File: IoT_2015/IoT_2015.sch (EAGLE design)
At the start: 31 parts, among them Y1 ABLS-16.000MHZ-B4-T

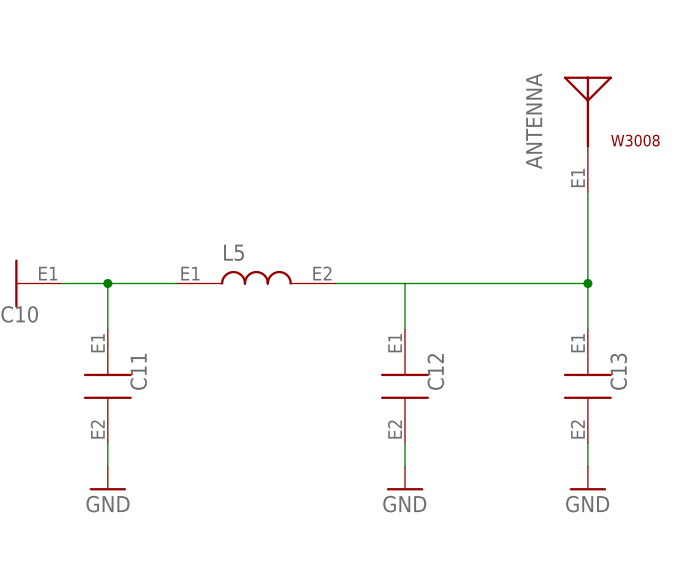
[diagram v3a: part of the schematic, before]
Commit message: Correction with ERC
Correction carried out with ERC
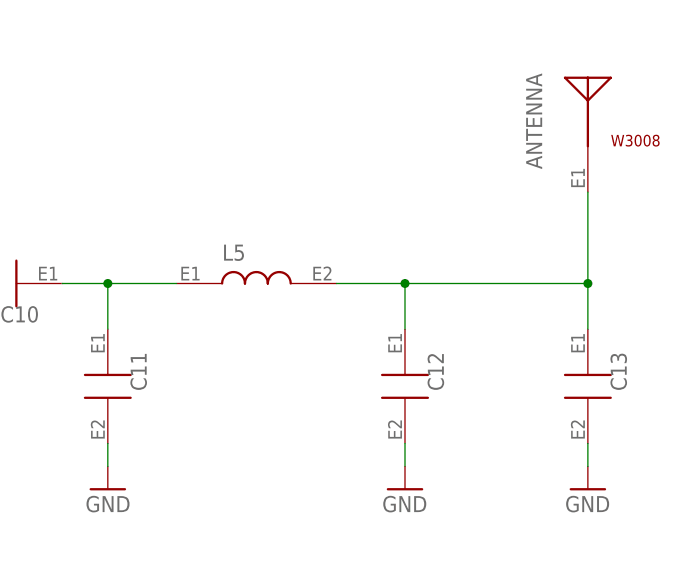
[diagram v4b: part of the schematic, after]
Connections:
- net GND: now also C13.E2
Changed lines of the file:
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@@
-</segment>
-<segment>
-<wire x1="307.34" y1="25.4" x2="307.34" y2="27.94" width="0.1524" layer="91"/>
 </segment>
 <segment>
@@
 <pinref part="R2" gate="G$1" pin="E1"/>
 <pinref part="GND13" gate="1" pin="GND"/>
+</segment>
+<segment>
+<pinref part="GND12" gate="1" pin="GND"/>
+<pinref part="C13" gate="G$1" pin="E2"/>
+<wire x1="307.34" y1="25.4" x2="307.34" y2="27.94" width="0.1524" layer="91"/>
 </segment>
 </net>
@@
 <wire x1="307.34" y1="45.72" x2="307.34" y2="55.88" width="0.1524" layer="91"/>
 <junction x="307.34" y="45.72"/>
+<junction x="287.02" y="45.72"/>
 </segment>
 </net>

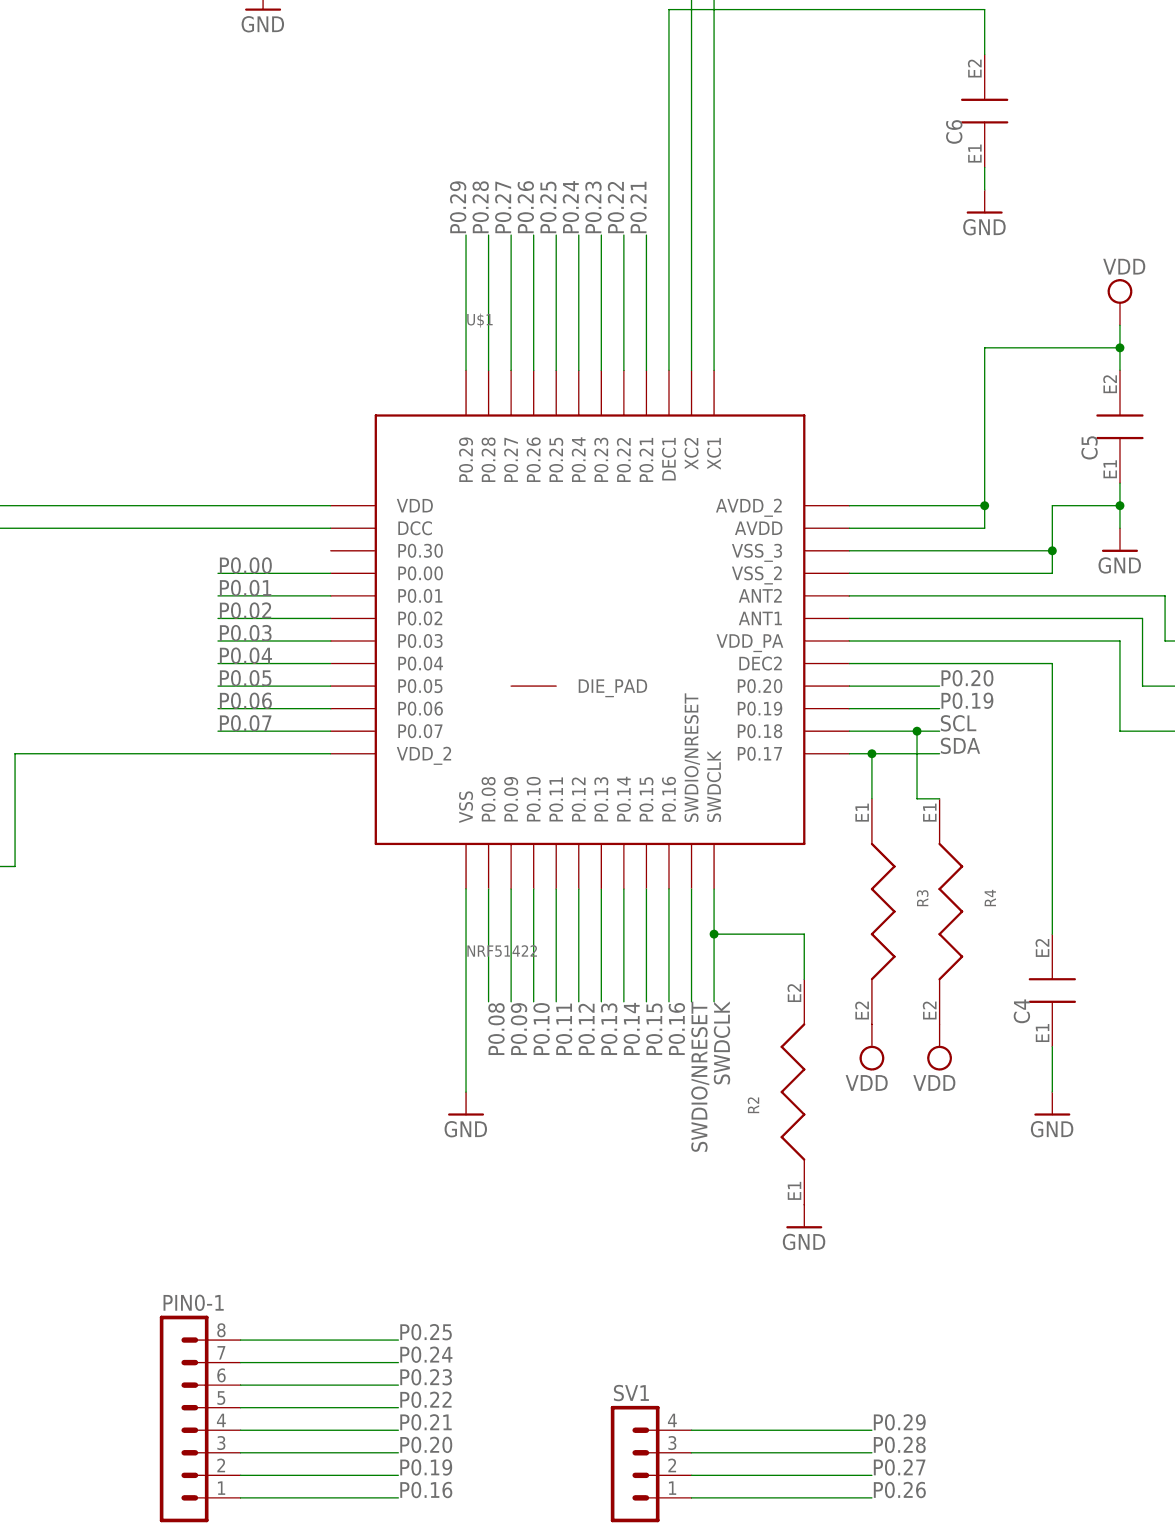
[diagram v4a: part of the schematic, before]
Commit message: BoardLayout
Fixed the layer-property of battery and started the board-layout.
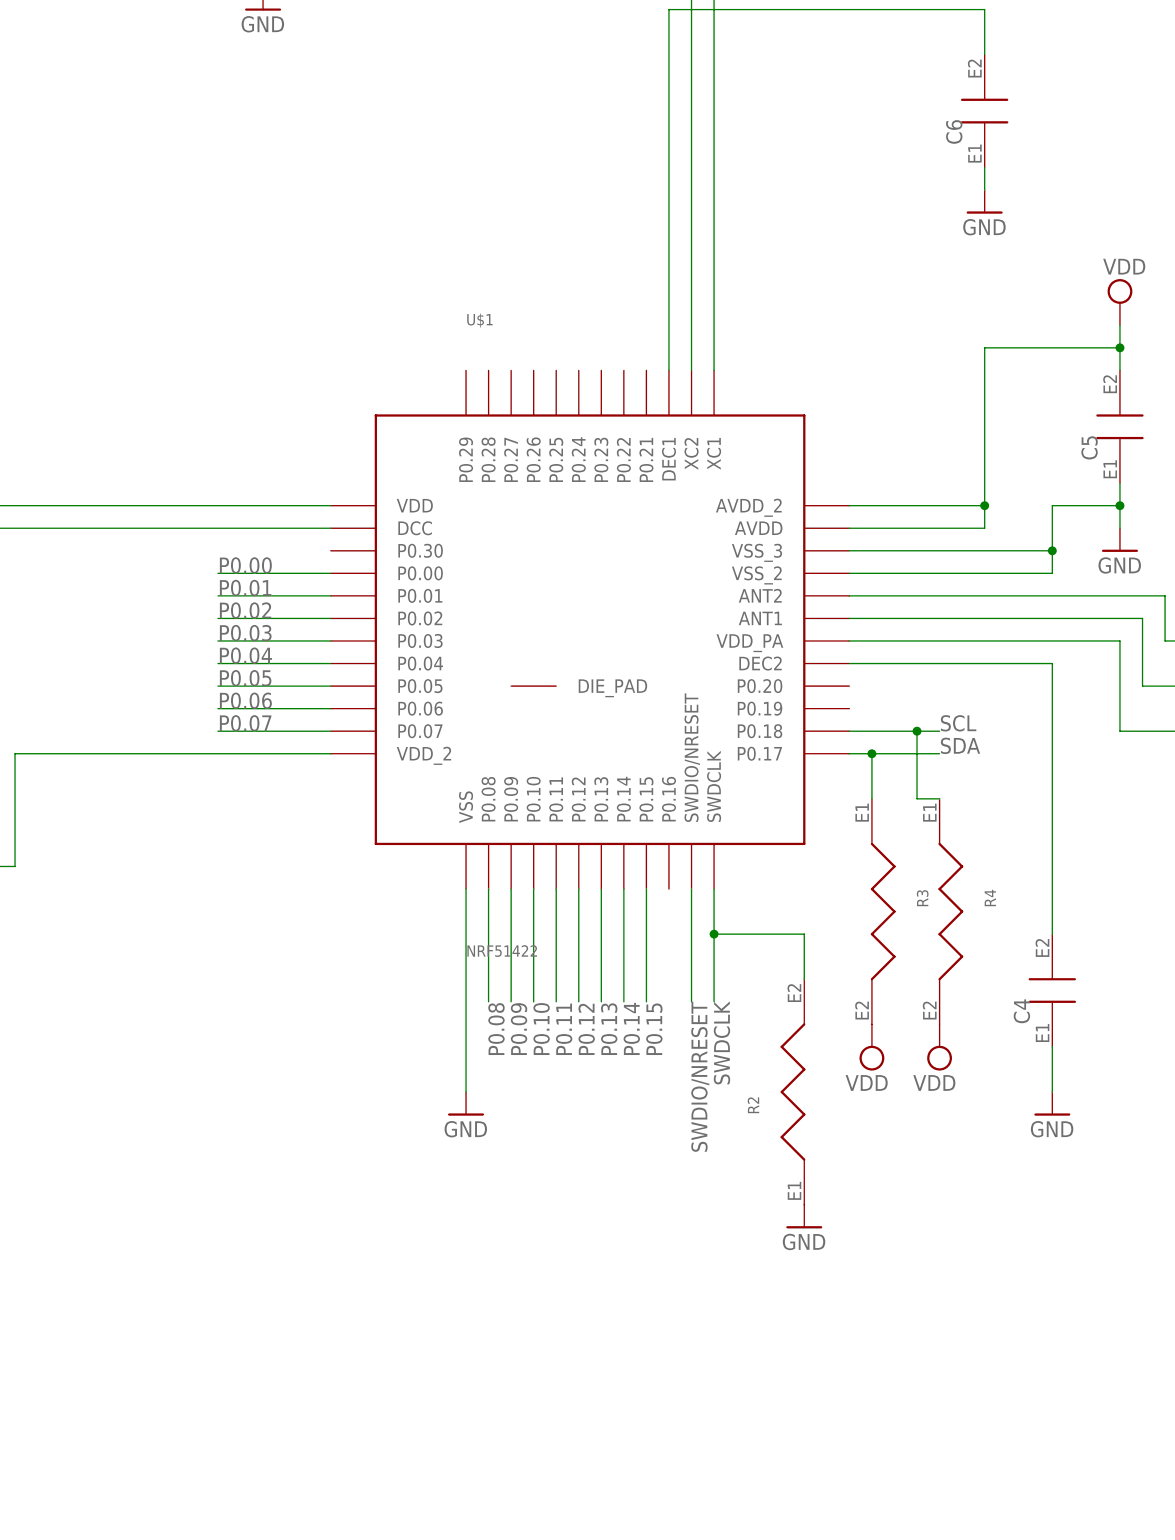
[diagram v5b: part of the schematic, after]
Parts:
- removed PIN0-1: (no value), con-lstb:MA08-1
- removed SV1: (no value), con-lstb:MA04-1
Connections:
- removed net P0.16: PIN0-1.1, U$1.P0.16
- removed net P0.19: PIN0-1.2, U$1.P0.19
- removed net P0.20: PIN0-1.3, U$1.P0.20
- removed net P0.21: PIN0-1.4, U$1.P0.21
- removed net P0.22: PIN0-1.5, U$1.P0.22
- removed net P0.23: PIN0-1.6, U$1.P0.23
- removed net P0.24: PIN0-1.7, U$1.P0.24
- removed net P0.25: PIN0-1.8, U$1.P0.25
- removed net P0.26: SV1.1, U$1.P0.26
- removed net P0.27: SV1.2, U$1.P0.27
- removed net P0.28: SV1.3, U$1.P0.28
- removed net P0.29: SV1.4, U$1.P0.29
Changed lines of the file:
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@@
 <part name="SUPPLY7" library="supply2" deviceset="VDD" device=""/>
 <part name="SUPPLY8" library="supply2" deviceset="VDD" device=""/>
-<part name="PIN0-1" library="con-lstb" deviceset="MA08-1" device=""/>
-<part name="SV1" library="con-lstb" deviceset="MA04-1" device=""/>
 </parts>
 <sheets>
@@
 <instance part="SUPPLY7" gate="G$1" x="129.54" y="0" rot="R180"/>
 <instance part="SUPPLY8" gate="G$1" x="137.16" y="0" rot="R180"/>
-<instance part="PIN0-1" gate="1" x="50.8" y="-43.18"/>
-<instance part="SV1" gate="1" x="101.6" y="-45.72"/>
 </instances>
 <busses>
@@
 </segment>
 </net>
-<net name="P0.16" class="0">
-<segment>
-<pinref part="U$1" gate="G$1" pin="P0.16"/>
-<wire x1="106.68" y1="17.78" x2="106.68" y2="5.08" width="0.1524" layer="91"/>
-<label x="106.68" y="5.08" size="1.778" layer="95" rot="R270"/>
-</segment>
-<segment>
-<pinref part="PIN0-1" gate="1" pin="1"/>
-<wire x1="58.42" y1="-50.8" x2="76.2" y2="-50.8" width="0.1524" layer="91"/>
-<label x="76.2" y="-50.8" size="1.778" layer="95"/>
-</segment>
-</net>
-<net name="P0.19" class="0">
-<segment>
-<pinref part="U$1" gate="G$1" pin="P0.19"/>
-<wire x1="127" y1="38.1" x2="137.16" y2="38.1" width="0.1524" layer="91"/>
-<label x="137.16" y="38.1" size="1.778" layer="95"/>
-</segment>
-<segment>
-<pinref part="PIN0-1" gate="1" pin="2"/>
-<wire x1="58.42" y1="-48.26" x2="76.2" y2="-48.26" width="0.1524" layer="91"/>
-<label x="76.2" y="-48.26" size="1.778" layer="95"/>
-</segment>
-</net>
-<net name="P0.20" class="0">
-<segment>
-<pinref part="U$1" gate="G$1" pin="P0.20"/>
-<wire x1="127" y1="40.64" x2="137.16" y2="40.64" width="0.1524" layer="91"/>
-<label x="137.16" y="40.64" size="1.778" layer="95"/>
-</segment>
-<segment>
-<pinref part="PIN0-1" gate="1" pin="3"/>
-<wire x1="58.42" y1="-45.72" x2="76.2" y2="-45.72" width="0.1524" layer="91"/>
-<label x="76.2" y="-45.72" size="1.778" layer="95"/>
-</segment>
-</net>
-<net name="P0.21" class="0">
-<segment>
-<pinref part="U$1" gate="G$1" pin="P0.21"/>
-<wire x1="104.14" y1="76.2" x2="104.14" y2="91.44" width="0.1524" layer="91"/>
-<label x="104.14" y="91.44" size="1.778" layer="95" rot="R90"/>
-</segment>
-<segment>
-<pinref part="PIN0-1" gate="1" pin="4"/>
-<wire x1="58.42" y1="-43.18" x2="76.2" y2="-43.18" width="0.1524" layer="91"/>
-<label x="76.2" y="-43.18" size="1.778" layer="95"/>
-</segment>
-</net>
-<net name="P0.22" class="0">
-<segment>
-<pinref part="U$1" gate="G$1" pin="P0.22"/>
-<wire x1="101.6" y1="76.2" x2="101.6" y2="91.44" width="0.1524" layer="91"/>
-<label x="101.6" y="91.44" size="1.778" layer="95" rot="R90"/>
-</segment>
-<segment>
-<pinref part="PIN0-1" gate="1" pin="5"/>
-<wire x1="58.42" y1="-40.64" x2="76.2" y2="-40.64" width="0.1524" layer="91"/>
-<label x="76.2" y="-40.64" size="1.778" layer="95"/>
-</segment>
-</net>
-<net name="P0.23" class="0">
-<segment>
-<pinref part="U$1" gate="G$1" pin="P0.23"/>
-<wire x1="99.06" y1="76.2" x2="99.06" y2="91.44" width="0.1524" layer="91"/>
-<label x="99.06" y="91.44" size="1.778" layer="95" rot="R90"/>
-</segment>
-<segment>
-<pinref part="PIN0-1" gate="1" pin="6"/>
-<wire x1="58.42" y1="-38.1" x2="76.2" y2="-38.1" width="0.1524" layer="91"/>
-<label x="76.2" y="-38.1" size="1.778" layer="95"/>
-</segment>
-</net>
-<net name="P0.24" class="0">
-<segment>
-<pinref part="U$1" gate="G$1" pin="P0.24"/>
-<wire x1="96.52" y1="76.2" x2="96.52" y2="91.44" width="0.1524" layer="91"/>
-<label x="96.52" y="91.44" size="1.778" layer="95" rot="R90"/>
-</segment>
-<segment>
-<pinref part="PIN0-1" gate="1" pin="7"/>
-<wire x1="58.42" y1="-35.56" x2="76.2" y2="-35.56" width="0.1524" layer="91"/>
-<label x="76.2" y="-35.56" size="1.778" layer="95"/>
-</segment>
-</net>
-<net name="P0.25" class="0">
-<segment>
-<pinref part="U$1" gate="G$1" pin="P0.25"/>
-<wire x1="93.98" y1="76.2" x2="93.98" y2="91.44" width="0.1524" layer="91"/>
-<label x="93.98" y="91.44" size="1.778" layer="95" rot="R90"/>
-</segment>
-<segment>
-<pinref part="PIN0-1" gate="1" pin="8"/>
-<wire x1="58.42" y1="-33.02" x2="76.2" y2="-33.02" width="0.1524" layer="91"/>
-<label x="76.2" y="-33.02" size="1.778" layer="95"/>
-</segment>
-</net>
-<net name="P0.26" class="0">
-<segment>
-<pinref part="U$1" gate="G$1" pin="P0.26"/>
-<wire x1="91.44" y1="76.2" x2="91.44" y2="91.44" width="0.1524" layer="91"/>
-<label x="91.44" y="91.44" size="1.778" layer="95" rot="R90"/>
-</segment>
-<segment>
-<wire x1="109.22" y1="-50.8" x2="129.54" y2="-50.8" width="0.1524" layer="91"/>
-<label x="129.54" y="-50.8" size="1.778" layer="95"/>
-<pinref part="SV1" gate="1" pin="1"/>
-</segment>
-</net>
-<net name="P0.27" class="0">
-<segment>
-<pinref part="U$1" gate="G$1" pin="P0.27"/>
-<wire x1="88.9" y1="76.2" x2="88.9" y2="91.44" width="0.1524" layer="91"/>
-<label x="88.9" y="91.44" size="1.778" layer="95" rot="R90"/>
-</segment>
-<segment>
-<wire x1="109.22" y1="-48.26" x2="129.54" y2="-48.26" width="0.1524" layer="91"/>
-<label x="129.54" y="-48.26" size="1.778" layer="95"/>
-<pinref part="SV1" gate="1" pin="2"/>
-</segment>
-</net>
-<net name="P0.28" class="0">
-<segment>
-<pinref part="U$1" gate="G$1" pin="P0.28"/>
-<wire x1="86.36" y1="76.2" x2="86.36" y2="91.44" width="0.1524" layer="91"/>
-<label x="86.36" y="91.44" size="1.778" layer="95" rot="R90"/>
-</segment>
-<segment>
-<wire x1="109.22" y1="-45.72" x2="129.54" y2="-45.72" width="0.1524" layer="91"/>
-<label x="129.54" y="-45.72" size="1.778" layer="95"/>
-<pinref part="SV1" gate="1" pin="3"/>
-</segment>
-</net>
-<net name="P0.29" class="0">
-<segment>
-<pinref part="U$1" gate="G$1" pin="P0.29"/>
-<wire x1="83.82" y1="76.2" x2="83.82" y2="91.44" width="0.1524" layer="91"/>
-<label x="83.82" y="91.44" size="1.778" layer="95" rot="R90"/>
-</segment>
-<segment>
-<wire x1="109.22" y1="-43.18" x2="129.54" y2="-43.18" width="0.1524" layer="91"/>
-<label x="129.54" y="-43.18" size="1.778" layer="95"/>
-<pinref part="SV1" gate="1" pin="4"/>
-</segment>
-</net>

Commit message: First board design finished
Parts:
- removed HUM/TEMP: SHTC1, Sensirion:SHTC1
- added SI7006: SI7006-A20-IM, SiliconLabs:SI7006-A20-IM
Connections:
- net GND: now also SI7006.GND; no longer HUM/TEMP.VSS
- net SCL: now also SI7006.SCL; no longer HUM/TEMP.SCL
- net SDA: now also SI7006.SDA; no longer HUM/TEMP.SDA
- net VDD: now also SI7006.VDD; no longer HUM/TEMP.VDD
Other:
- note added: "BlueNinc"
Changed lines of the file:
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@@
 <?xml version="1.0" encoding="utf-8"?>
 <!DOCTYPE eagle SYSTEM "eagle.dtd">
-<eagle version="7.2.0">
+<eagle version="7.3.0">
 <drawing>
 <settings>
@@
 <part name="GND13" library="supply1" deviceset="GND" device=""/>
 <part name="JTAG" library="con-lstb" deviceset="MA03-1" device=""/>
-<part name="HUM/TEMP" library="Sensirion" deviceset="SHTC1" device=""/>
-<part name="SUPPLY5" library="supply2" deviceset="VDD" device=""/>
-<part name="GND14" library="supply1" deviceset="GND" device=""/>
 <part name="ANTENNA" library="Pulse" deviceset="W3008" device=""/>
 <part name="BATTERY" library="Renata" deviceset="SMTU2032-G.TR" device=""/>
@@
 <part name="SUPPLY7" library="supply2" deviceset="VDD" device=""/>
 <part name="SUPPLY8" library="supply2" deviceset="VDD" device=""/>
+<part name="SI7006" library="SiliconLabs" deviceset="SI7006-A20-IM" device=""/>
+<part name="GND17" library="supply1" deviceset="GND" device=""/>
+<part name="SUPPLY5" library="supply2" deviceset="VDD" device=""/>
 </parts>
 <sheets>
 <sheet>
 <plain>
+<text x="289.56" y="-55.88" size="1.778" layer="91">BlueNinc</text>
 </plain>
 <instances>
@@
 <instance part="GND13" gate="1" x="121.92" y="-20.32"/>
 <instance part="JTAG" gate="G$1" x="-43.18" y="-43.18"/>
-<instance part="HUM/TEMP" gate="G$1" x="-25.4" y="124.46"/>
-<instance part="SUPPLY5" gate="G$1" x="-38.1" y="147.32"/>
-<instance part="GND14" gate="1" x="17.78" y="142.24"/>
 <instance part="ANTENNA" gate="G$1" x="307.34" y="60.96"/>
 <instance part="BATTERY" gate="G$1" x="294.64" y="142.24"/>
@@
 <instance part="SUPPLY7" gate="G$1" x="129.54" y="0" rot="R180"/>
 <instance part="SUPPLY8" gate="G$1" x="137.16" y="0" rot="R180"/>
+<instance part="SI7006" gate="G$1" x="-12.7" y="104.14" rot="R90"/>
+<instance part="GND17" gate="1" x="-33.02" y="104.14" rot="R270"/>
+<instance part="SUPPLY5" gate="G$1" x="7.62" y="104.14" rot="R270"/>
 </instances>
 <busses>
@@
 </segment>
 <segment>
-<pinref part="HUM/TEMP" gate="G$1" pin="VDD"/>
-<wire x1="-30.48" y1="144.78" x2="-38.1" y2="144.78" width="0.1524" layer="91"/>
-<pinref part="SUPPLY5" gate="G$1" pin="VDD"/>
-</segment>
-<segment>
 <pinref part="BATTERY" gate="G$1" pin="VCC"/>
 <wire x1="294.64" y1="149.86" x2="294.64" y2="157.48" width="0.1524" layer="91"/>
@@
 <pinref part="R4" gate="G$1" pin="E2"/>
 <pinref part="SUPPLY8" gate="G$1" pin="VDD"/>
+</segment>
+<segment>
+<pinref part="SI7006" gate="G$1" pin="VDD"/>
+<wire x1="-5.08" y1="104.14" x2="5.08" y2="104.14" width="0.1524" layer="91"/>
+<pinref part="SUPPLY5" gate="G$1" pin="VDD"/>
 </segment>
 </net>
@@
 </segment>
 <segment>
-<pinref part="HUM/TEMP" gate="G$1" pin="VSS"/>
-<wire x1="10.16" y1="144.78" x2="17.78" y2="144.78" width="0.1524" layer="91"/>
-<pinref part="GND14" gate="1" pin="GND"/>
-</segment>
-<segment>
 <pinref part="BATTERY" gate="G$1" pin="GND"/>
 <wire x1="294.64" y1="137.16" x2="294.64" y2="129.54" width="0.1524" layer="91"/>
@@
 <pinref part="C13" gate="G$1" pin="E2"/>
 <wire x1="307.34" y1="25.4" x2="307.34" y2="27.94" width="0.1524" layer="91"/>
+</segment>
+<segment>
+<pinref part="SI7006" gate="G$1" pin="GND"/>
+<wire x1="-20.32" y1="104.14" x2="-30.48" y2="104.14" width="0.1524" layer="91"/>
+<pinref part="GND17" gate="1" pin="GND"/>
 </segment>
 </net>
@@
 <net name="SDA" class="0">
 <segment>
-<pinref part="HUM/TEMP" gate="G$1" pin="SDA"/>
-<wire x1="10.16" y1="129.54" x2="17.78" y2="129.54" width="0.1524" layer="91"/>
-<label x="17.78" y="129.54" size="1.778" layer="95"/>
-</segment>
-<segment>
 <pinref part="U$1" gate="G$1" pin="P0.17"/>
 <wire x1="127" y1="33.02" x2="129.54" y2="33.02" width="0.1524" layer="91"/>
@@
 <junction x="129.54" y="33.02"/>
 </segment>
+<segment>
+<pinref part="SI7006" gate="G$1" pin="SDA"/>
+<wire x1="-20.32" y1="109.22" x2="-30.48" y2="109.22" width="0.1524" layer="91"/>
+<label x="-30.48" y="109.22" size="1.778" layer="95" rot="R180"/>
+</segment>
 </net>
 <net name="SCL" class="0">
-<segment>
-<pinref part="HUM/TEMP" gate="G$1" pin="SCL"/>
-<wire x1="-30.48" y1="129.54" x2="-38.1" y2="129.54" width="0.1524" layer="91"/>
-<label x="-38.1" y="129.54" size="1.778" layer="95"/>
-</segment>
 <segment>
 <pinref part="U$1" gate="G$1" pin="P0.18"/>
@@
 <junction x="134.62" y="35.56"/>
 </segment>
+<segment>
+<pinref part="SI7006" gate="G$1" pin="SCL"/>
+<wire x1="-5.08" y1="109.22" x2="5.08" y2="109.22" width="0.1524" layer="91"/>
+<label x="5.08" y="109.22" size="1.778" layer="95"/>
+</segment>
 </net>
 </nets>
 </sheet>
 </sheets>
+<errors>
+</errors>
 </schematic>
 </drawing>
